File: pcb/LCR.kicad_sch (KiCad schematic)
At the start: 44 parts, among them J1 Conn_01x02_Pin, J2 USB_C_Receptacle, Q1 BSP613, SW1 SW_SPDT, U1 LM1117DT-3.3, U2 TPS61023DRLR

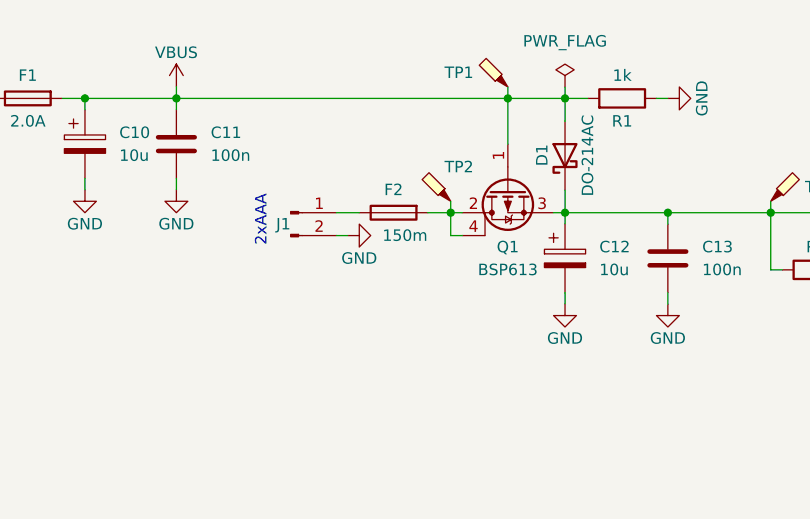
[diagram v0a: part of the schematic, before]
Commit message: Add/fix missing/wrong vendor(id)
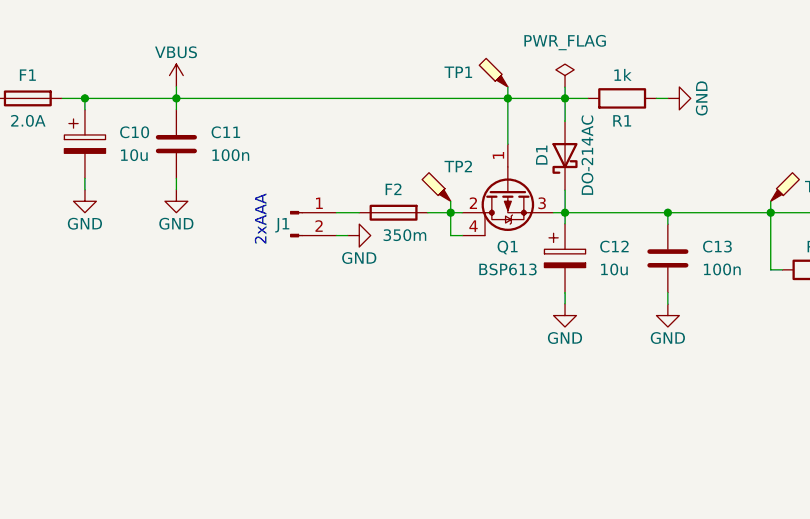
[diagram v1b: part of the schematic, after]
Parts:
- F2: value 150m -> 350m; VendorId (none) -> 101639
- H1: Vendor HTL -> (none); VendorId 101017, 101382 -> (none)
- U1: Vendor (none) -> HTL; VendorId (none) -> 103444
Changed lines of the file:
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@@
       (effects (font (size 1.27 1.27)) hide)
     )
-    (property "Vendor" "HTL" (at 262.89 149.86 0)
-      (effects (font (size 1.27 1.27)) hide)
-    )
-    (property "VendorId" "101017, 101382" (at 262.89 149.86 0)
+    (property "Vendor" "" (at 262.89 149.86 0)
+      (effects (font (size 1.27 1.27)) hide)
+    )
+    (property "VendorId" "" (at 262.89 149.86 0)
       (effects (font (size 1.27 1.27)) hide)
     )
@@
       (effects (font (size 1.27 1.27)))
     )
-    (property "Value" "150m" (at 120.65 88.9 90)
+    (property "Value" "350m" (at 120.65 88.9 90)
       (effects (font (size 1.27 1.27)))
     )
@@
       (effects (font (size 1.27 1.27)) hide)
     )
-    (property "VendorId" "" (at 119.38 86.36 0)
+    (property "VendorId" "101639" (at 119.38 86.36 0)
       (effects (font (size 1.27 1.27)) hide)
     )
@@
       (effects (font (size 1.27 1.27)) hide)
     )
+    (property "Vendor" "HTL" (at 242.57 86.36 0)
+      (effects (font (size 1.27 1.27)) hide)
+    )
+    (property "VendorId" "103444" (at 242.57 86.36 0)
+      (effects (font (size 1.27 1.27)) hide)
+    )

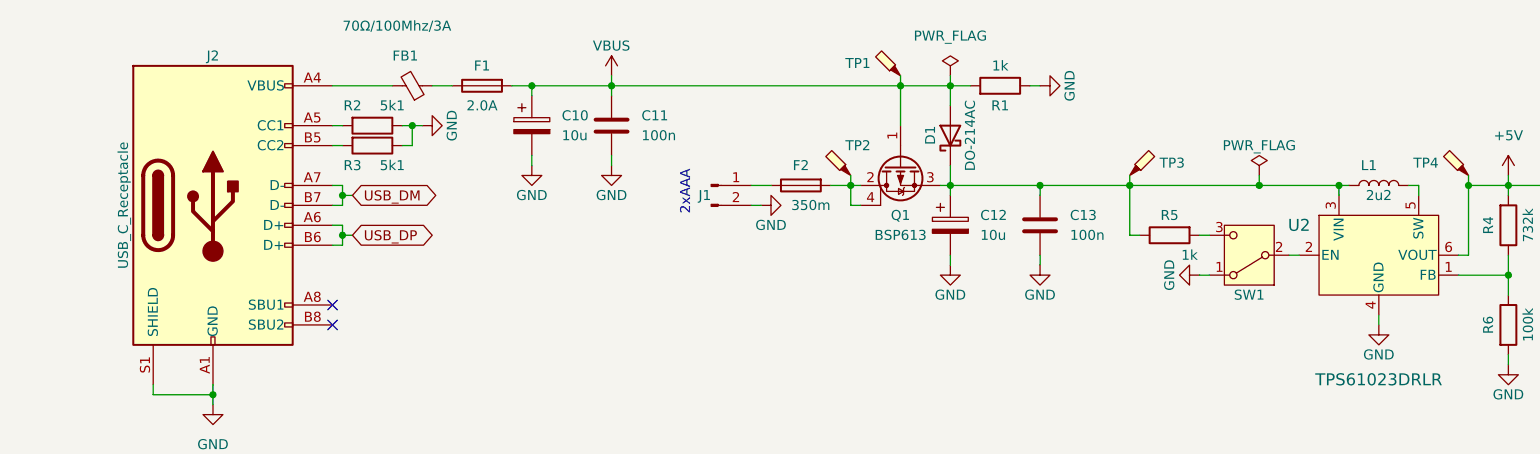
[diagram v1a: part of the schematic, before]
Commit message: Change MCP2221A to FT230X
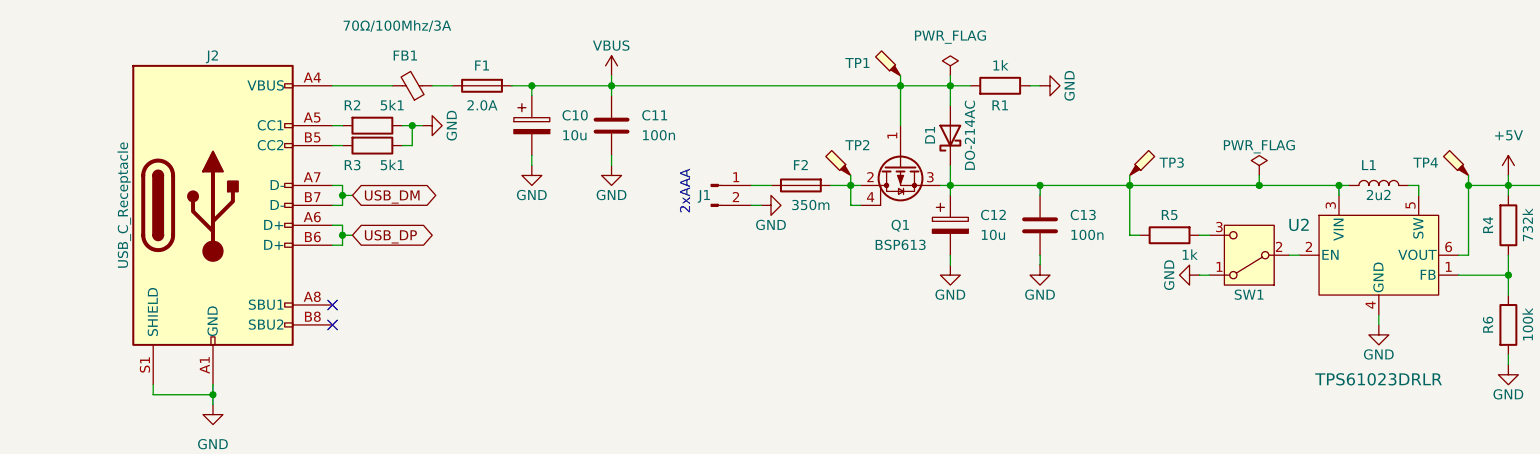
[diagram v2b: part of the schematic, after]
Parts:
- removed Q1: BSP613, Package_TO_SOT_SMD:SOT-223, symbol Device:Q_PMOS_GDSD
- added Q1: BSP613, Package_TO_SOT_SMD:SOT-223, symbol Transistor_FET:Q_PMOS_GDSD
- FID1, FID2, FID3, FID4: now left out of the parts list
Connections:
- net VBUS: now also Q1.1 (G)
- net at C12.1, C13.1, D1.1 (K)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: now also Q1.3 (S)
- net at F2.2, TP2.1: now also Q1.2 (D), Q1.4 (D)

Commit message: Rename/Add/Remove bom fields
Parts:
- C1, C10, C12, C14, C16, C2: HTL (none) -> 103620; Vendor HTL -> (none); VendorId 103620 -> (none)
- C11, C13, C15, C3, C4, C5, C6, C7, C8, C9: HTL (none) -> 100128; Vendor HTL -> (none); VendorId 100128 -> (none)
- D1: HTL (none) -> 103360; Vendor HTL -> (none); VendorId 103360 -> (none)
- D2: HTL (none) -> 100189; Vendor HTL -> (none); VendorId 100189 -> (none)
- F1: HTL (none) -> 103597; Vendor HTL -> (none); VendorId 103597 -> (none)
- F2: HTL (none) -> 101639; Vendor HTL -> (none); VendorId 101639 -> (none)
- FB1: HTL (none) -> 103570; Vendor HTL -> (none); VendorId 103570 -> (none)
- J1: HTL (none) -> 103599; Vendor HTL -> (none); VendorId 103599 -> (none)
- J2: HTL (none) -> 103572; Vendor HTL -> (none); VendorId 103572 -> (none)
- L1: HTL (none) -> 103600; Vendor HTL -> (none); VendorId 103600 -> (none)
- Q1: HTL (none) -> 103601
- R1, R5: HTL (none) -> 102951; Vendor HTL -> (none); VendorId 102951 -> (none)
- R2, R3: HTL (none) -> 102962; Vendor HTL -> (none); VendorId 102962 -> (none)
- R4: HTL (none) -> 103602; Vendor HTL -> (none); VendorId 103602 -> (none)
- R6: HTL (none) -> 102987; Vendor HTL -> (none); VendorId 102987 -> (none)
- SW1: HTL (none) -> 103603; Vendor HTL -> (none); VendorId 103603 -> (none)
- TP1, TP2, TP3, TP4, TP5: now left out of the parts list
- U1: HTL (none) -> 103444; Vendor HTL -> (none); VendorId 103444 -> (none)
- U2: HTL (none) -> 103606; Vendor HTL -> (none); VendorId 103606 -> (none)
